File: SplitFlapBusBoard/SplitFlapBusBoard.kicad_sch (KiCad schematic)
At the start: 2 parts, among them J1 Conn_01x04_Pin, J2 Conn_01x04_Pin

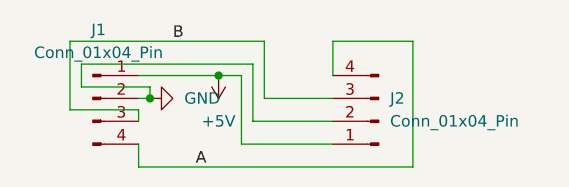
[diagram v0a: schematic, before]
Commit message: Version 2 of Hub and Module Board
Finished and ordered bus board and V2 or Module board (50x)
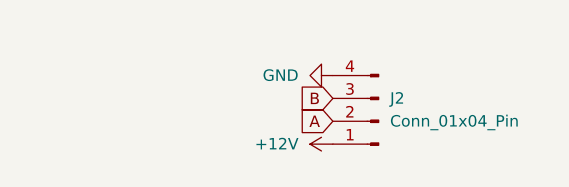
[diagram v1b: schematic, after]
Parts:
- removed J1: Conn_01x04_Pin, Connector_PinHeader_2.54mm:PinHeader_1x04_P2.54mm_Vertical, symbol Connector:Conn_01x04_Pin
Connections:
- net A: now also J2.2 (Pin_2); no longer J2.4 (Pin_4)
- net GND: now also J2.4 (Pin_4); no longer J2.2 (Pin_2)
- net +5V renamed +12V
